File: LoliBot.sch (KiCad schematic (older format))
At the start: 41 parts, among them J1 LOLINBATT, J10 LEFT-MOTOR, J11 REFLECT_, J12 MECH, J13 MECH, J14 MECH, J15 MECH, J16 MECH, J17 MECH, J18 MECH, J19 MECH, J2 APA106, J20 CONN_01X08, J21 CONN_01X06, J3 SERVO1, J4 RIGHT, J5 LEFT, J6 MPU-9250, J7 APA106, J8 APA106, J9 RIGHT-MOTOR, SW1 SPST, U1 LOLIN32-LITE, U2 RT9276, U3 L9110, U4 L9110

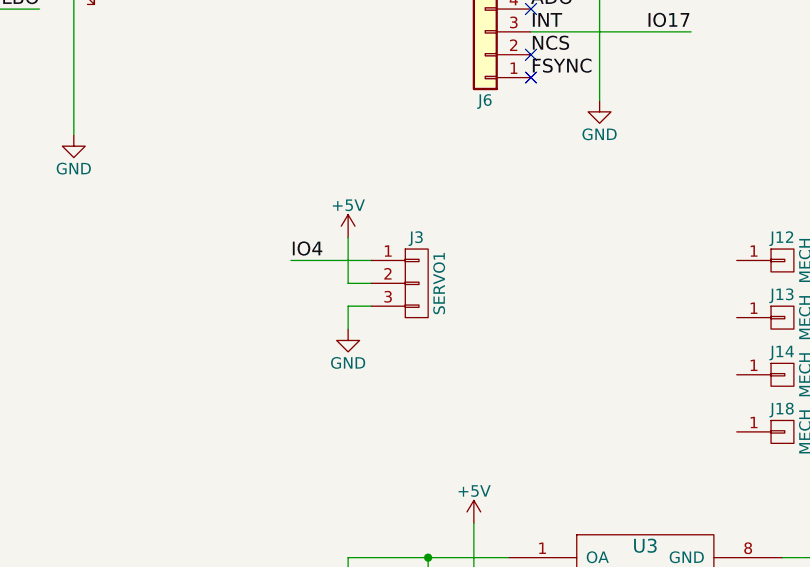
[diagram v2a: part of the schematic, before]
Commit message: Moved Servo position
to remove interference with expansion ports.
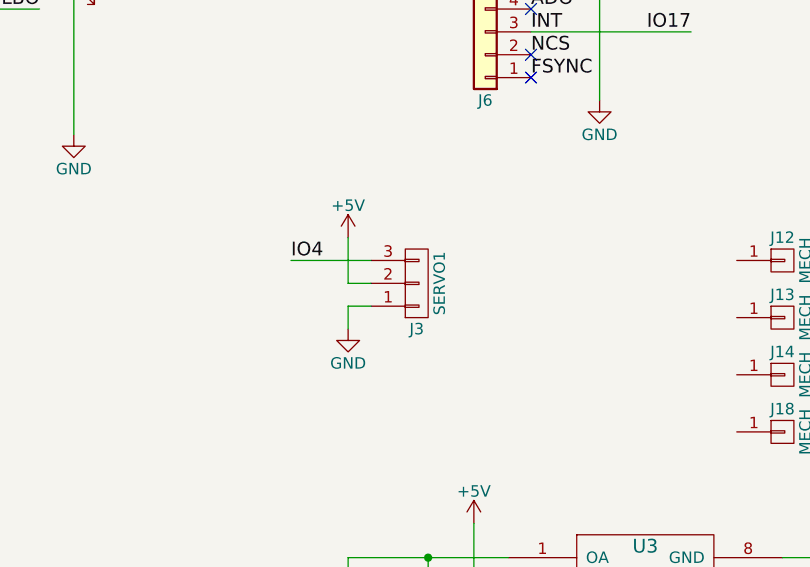
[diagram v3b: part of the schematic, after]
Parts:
- J3: footprint Pin_Headers:Pin_Header_Straight_1x03_Pitch2.54mm -> Pin_Headers:Pin_Header_Angled_1x03_Pitch2.54mm
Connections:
- net GND: now also J3.1 (P1); no longer J3.3 (P3)
- net IO4: now also J3.3 (P3); no longer J3.1 (P1)
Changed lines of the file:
@@
 F 0 "J3" H 8700 3100 50  0000 C CNN
 F 1 "SERVO1" V 8800 2900 50  0000 C CNN
-F 2 "Pin_Headers:Pin_Header_Straight_1x03_Pitch2.54mm" H 8700 2900 50  0001 C CNN
+F 2 "Pin_Headers:Pin_Header_Angled_1x03_Pitch2.54mm" H 8700 2900 50  0001 C CNN
 F 3 "" H 8700 2900 50  0001 C CNN
 	1    8700 2900
-	1    0    0    -1
+	1    0    0    1
 $EndComp
 $Comp

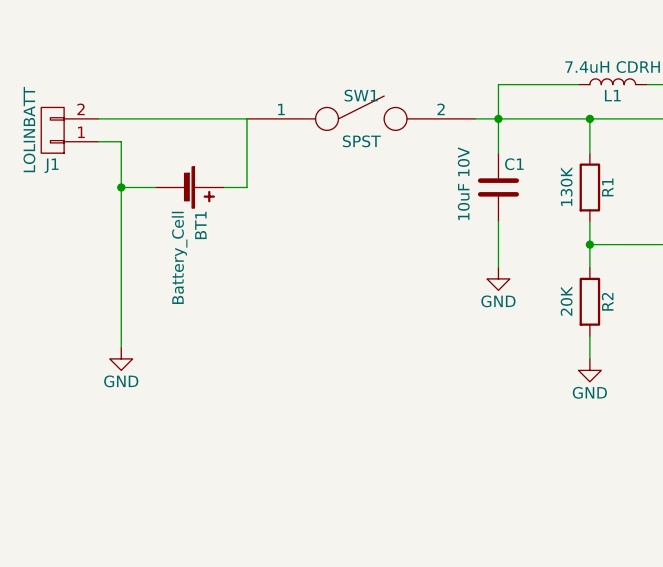
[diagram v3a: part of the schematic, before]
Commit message: battery symbols reversed.
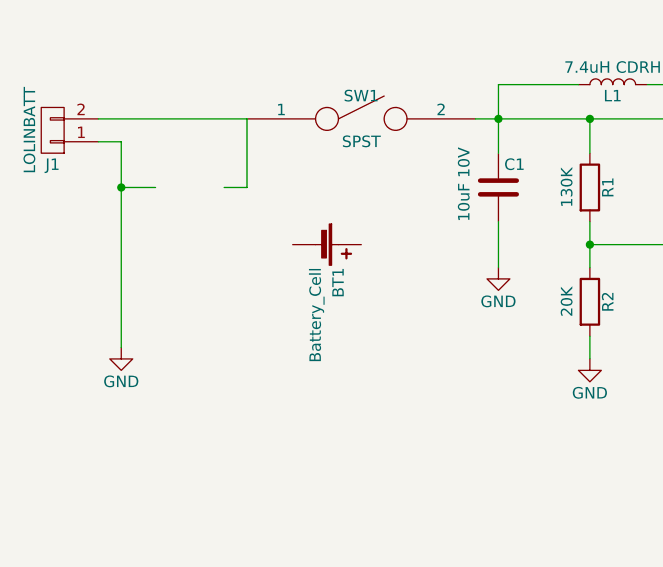
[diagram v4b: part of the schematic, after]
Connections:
- net GND: no longer BT1.2 (-)
- net at J1.2 (P2), SW1.1: no longer BT1.1 (+)
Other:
- moved on the sheet: BT1
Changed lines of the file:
@@
 L Battery_Cell BT1
 U 1 1 59DB5FBF
-P 1500 1450
-F 0 "BT1" H 1600 1550 50  0000 L CNN
-F 1 "Battery_Cell" H 1600 1450 50  0000 L CNN
-F 2 "libs:BH-18650" V 1500 1510 50  0001 C CNN
-F 3 "" V 1500 1510 50  0001 C CNN
-	1    1500 1450
+P 2100 1700
+F 0 "BT1" H 2200 1800 50  0000 L CNN
+F 1 "Battery_Cell" H 2200 1700 50  0000 L CNN
+F 2 "libs:BH-18650" V 2100 1760 50  0001 C CNN
+F 3 "" V 2100 1760 50  0001 C CNN
+	1    2100 1700
 	0    1    1    0
 $EndComp

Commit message: Removed voltage boost.
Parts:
- removed C1: 10uF 10V, Capacitors_SMD:C_1210_HandSoldering, symbol C
- removed C2: 22uF 10V, Capacitors_SMD:C_1210_HandSoldering, symbol C
- removed D1: LOW BATT, LEDs:LED_D3.0mm, symbol LED
- removed L1: 7.4uH CDRH, Choke_SMD:Choke_SMD_7.3x7.3_H3.5, symbol L
- removed R1: 130K, Resistors_SMD:R_0805_HandSoldering, symbol R
- removed R2: 20K, Resistors_SMD:R_0805_HandSoldering, symbol R
- removed R3: 180K 1%, Resistors_SMD:R_0805_HandSoldering, symbol R
- removed R4: 20K 1%, Resistors_SMD:R_0805_HandSoldering, symbol R
- removed R5: 10K, Resistors_SMD:R_0805_HandSoldering, symbol R
- removed R6: 1K, Resistors_SMD:R_0805_HandSoldering, symbol R
- removed U2: RT9276, Housings_DFN_QFN:DFN-10-1EP_3x3mm_Pitch0.5mm, symbol RT9276
- added J22, J23: BRIDGE, Pin_Headers:Pin_Header_Straight_1x02_Pitch2.54mm, symbol CONN_01X02
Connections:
- net GND: now also BT1.2 (-)
- net IO16: now also J3.3 (P3); no longer J11.3 (P3)
- net IO4: now also J11.3 (P3); no longer J3.3 (P3)
- net BATT_V: now reaches J1.2 (P2), SW1.1
- net BATT_V: now also J2.2 (P2), J20.1 (P1), J3.2 (P2), J7.2 (P2), J8.2 (P2), R7.1, J22.1 (P1), J23.1 (P1)
- net at BT1.1 (+): now also SW1.2
- removed net +5V: J2.2 (P2), J20.1 (P1), J3.2 (P2), J7.2 (P2), J8.2 (P2), R7.1, U3.2 (VCC), U3.3 (VCC), U4.2 (VCC), U4.3 (VCC)
- new net: J22.2 (P2), U3.2 (VCC), U3.3 (VCC)
- new net: J23.2 (P2), U4.2 (VCC), U4.3 (VCC)
- no-connect marks 9 -> 16
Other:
- note removed: "Vout = 5.0V\nat 500mA max."
- moved on the sheet: BT1, C4, J5, U4

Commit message: Added Fuse.  Updated pcb
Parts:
- added F1: 1A PTC, Resistors_SMD:R_1210_HandSoldering, symbol Polyfuse
- added J24: FUSE_BRIDGE, libs:bridge, symbol CONN_01X02
- added J25, J26: MECH, Mounting_Holes:MountingHole_3.2mm_M3_Pad, symbol CONN_01X01
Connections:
- net +3V3: no longer J11.1 (P1)
- net IO22: now also J11.1 (P1)
- net at BT1.1 (+): now also F1.2, J24.2 (P2); no longer SW1.2
- new net: F1.1, J24.1 (P1), SW1.2
- no-connect marks 16 -> 18
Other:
- moved on the sheet: J12, J13, J14, J15, J16, J17, J18, J19
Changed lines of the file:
@@
 	1400 1450 1250 1450
 Connection ~ 1250 1450
-Wire Wire Line
-	1700 1450 2850 1450
 $Comp
 L SPST SW1
@@
 	5150 3350 5150 3550
 $Comp
-L GND #PWR012
+L GND #PWR011
 U 1 1 59E30F3C
 P 5150 3550
-F 0 "#PWR012" H 5150 3300 50  0001 C CNN
+F 0 "#PWR011" H 5150 3300 50  0001 C CNN
 F 1 "GND" H 5150 3400 50  0000 C CNN
 F 2 "" H 5150 3550 50  0001 C CNN
@@
 	6100 3350 6100 3550
 $Comp
-L GND #PWR014
+L GND #PWR012
 U 1 1 59F090C3
 P 6100 3550
-F 0 "#PWR014" H 6100 3300 50  0001 C CNN
+F 0 "#PWR012" H 6100 3300 50  0001 C CNN
 F 1 "GND" H 6100 3400 50  0000 C CNN
 F 2 "" H 6100 3550 50  0001 C CNN
@@
 L CONN_01X01 J15
 U 1 1 59F9BFEA
-P 10700 2800
-F 0 "J15" H 10700 2900 50  0000 C CNN
-F 1 "MECH" V 10800 2800 50  0000 C CNN
-F 2 "Mounting_Holes:MountingHole_3.2mm_M3_Pad" H 10700 2800 50  0001 C CNN
-F 3 "" H 10700 2800 50  0001 C CNN
-	1    10700 2800
+P 10700 2900
+F 0 "J15" H 10700 3000 50  0000 C CNN
+F 1 "MECH" V 10800 2900 50  0000 C CNN
+F 2 "Mounting_Holes:MountingHole_3.2mm_M3_Pad" H 10700 2900 50  0001 C CNN
+F 3 "" H 10700 2900 50  0001 C CNN
+	1    10700 2900
 	1    0    0    -1
 $EndComp
@@
 L CONN_01X01 J16
 U 1 1 59F9C210
-P 10700 3050
-F 0 "J16" H 10700 3150 50  0000 C CNN
-F 1 "MECH" V 10800 3050 50  0000 C CNN
-F 2 "Mounting_Holes:MountingHole_3.2mm_M3_Pad" H 10700 3050 50  0001 C CNN
-F 3 "" H 10700 3050 50  0001 C CNN
-	1    10700 3050
+P 10700 3150
+F 0 "J16" H 10700 3250 50  0000 C CNN
+F 1 "MECH" V 10800 3150 50  0000 C CNN
+F 2 "Mounting_Holes:MountingHole_3.2mm_M3_Pad" H 10700 3150 50  0001 C CNN
+F 3 "" H 10700 3150 50  0001 C CNN
+	1    10700 3150
 	1    0    0    -1
 $EndComp
@@
 L CONN_01X01 J12
 U 1 1 59F9C63A
-P 10300 2800
-F 0 "J12" H 10300 2900 50  0000 C CNN
-F 1 "MECH" V 10400 2800 50  0000 C CNN
-F 2 "Mounting_Holes:MountingHole_3.2mm_M3_Pad" H 10300 2800 50  0001 C CNN
-F 3 "" H 10300 2800 50  0001 C CNN
-	1    10300 2800
+P 10300 2900
+F 0 "J12" H 10300 3000 50  0000 C CNN
+F 1 "MECH" V 10400 2900 50  0000 C CNN
+F 2 "Mounting_Holes:MountingHole_3.2mm_M3_Pad" H 10300 2900 50  0001 C CNN
+F 3 "" H 10300 2900 50  0001 C CNN
+	1    10300 2900
 	1    0    0    -1
 $EndComp
@@
 L CONN_01X01 J13
 U 1 1 59F9C640
-P 10300 3050
-F 0 "J13" H 10300 3150 50  0000 C CNN
-F 1 "MECH" V 10400 3050 50  0000 C CNN
-F 2 "Mounting_Holes:MountingHole_3.2mm_M3_Pad" H 10300 3050 50  0001 C CNN
-F 3 "" H 10300 3050 50  0001 C CNN
-	1    10300 3050
+P 10300 3150
+F 0 "J13" H 10300 3250 50  0000 C CNN
+F 1 "MECH" V 10400 3150 50  0000 C CNN
+F 2 "Mounting_Holes:MountingHole_3.2mm_M3_Pad" H 10300 3150 50  0001 C CNN
+F 3 "" H 10300 3150 50  0001 C CNN
+	1    10300 3150
 	1    0    0    -1
 $EndComp
@@
 L CONN_01X01 J17
 U 1 1 59F9C6E4
-P 10700 3300
-F 0 "J17" H 10700 3400 50  0000 C CNN
-F 1 "MECH" V 10800 3300 50  0000 C CNN
-F 2 "Mounting_Holes:MountingHole_3.2mm_M3_Pad" H 10700 3300 50  0001 C CNN
-F 3 "" H 10700 3300 50  0001 C CNN
-	1    10700 3300
+P 10700 3400
+F 0 "J17" H 10700 3500 50  0000 C CNN
+F 1 "MECH" V 10800 3400 50  0000 C CNN
+F 2 "Mounting_Holes:MountingHole_3.2mm_M3_Pad" H 10700 3400 50  0001 C CNN
+F 3 "" H 10700 3400 50  0001 C CNN
+	1    10700 3400
 	1    0    0    -1
 $EndComp
@@
 L CONN_01X01 J14
 U 1 1 59F9C6EA
-P 10300 3300
-F 0 "J14" H 10300 3400 50  0000 C CNN
-F 1 "MECH" V 10400 3300 50  0000 C CNN
-F 2 "Mounting_Holes:MountingHole_3.2mm_M3_Pad" H 10300 3300 50  0001 C CNN
-F 3 "" H 10300 3300 50  0001 C CNN
-	1    10300 3300
+P 10300 3400
+F 0 "J14" H 10300 3500 50  0000 C CNN
+F 1 "MECH" V 10400 3400 50  0000 C CNN
+F 2 "Mounting_Holes:MountingHole_3.2mm_M3_Pad" H 10300 3400 50  0001 C CNN
+F 3 "" H 10300 3400 50  0001 C CNN
+	1    10300 3400
 	1    0    0    -1
 $EndComp
@@
 $EndComp
 $Comp
-L +3.3V #PWR015
-U 1 1 59F9D53B
-P 7150 5450
-F 0 "#PWR015" H 7150 5300 50  0001 C CNN
-F 1 "+3.3V" H 7150 5590 50  0000 C CNN
-F 2 "" H 7150 5450 50  0001 C CNN
-F 3 "" H 7150 5450 50  0001 C CNN
-	1    7150 5450
-	1    0    0    -1
-$EndComp
-$Comp
-L GND #PWR016
+L GND #PWR013
 U 1 1 59F9DB04
 P 7200 5850
-F 0 "#PWR016" H 7200 5600 50  0001 C CNN
+F 0 "#PWR013" H 7200 5600 50  0001 C CNN
 F 1 "GND" H 7200 5700 50  0000 C CNN
 F 2 "" H 7200 5850 50  0001 C CNN
@@
 $EndComp
 Wire Wire Line
-	7100 5500 7150 5500
-Wire Wire Line
-	7150 5500 7150 5450
-Wire Wire Line
 	7100 5600 7200 5600
 Wire Wire Line
@@
 L CONN_01X01 J19
 U 1 1 59F9F795
-P 10700 3550
-F 0 "J19" H 10700 3650 50  0000 C CNN
-F 1 "MECH" V 10800 3550 50  0000 C CNN
-F 2 "Mounting_Holes:MountingHole_3.2mm_M3_Pad" H 10700 3550 50  0001 C CNN
-F 3 "" H 10700 3550 50  0001 C CNN
-	1    10700 3550
+P 10700 3650
+F 0 "J19" H 10700 3750 50  0000 C CNN
+F 1 "MECH" V 10800 3650 50  0000 C CNN
+F 2 "Mounting_Holes:MountingHole_3.2mm_M3_Pad" H 10700 3650 50  0001 C CNN
+F 3 "" H 10700 3650 50  0001 C CNN
+	1    10700 3650
 	1    0    0    -1
 $EndComp
@@
 L CONN_01X01 J18
 U 1 1 59F9F79B
-P 10300 3550
-F 0 "J18" H 10300 3650 50  0000 C CNN
-F 1 "MECH" V 10400 3550 50  0000 C CNN
-F 2 "Mounting_Holes:MountingHole_3.2mm_M3_Pad" H 10300 3550 50  0001 C CNN
-F 3 "" H 10300 3550 50  0001 C CNN
-	1    10300 3550
+P 10300 3650
+F 0 "J18" H 10300 3750 50  0000 C CNN
+F 1 "MECH" V 10400 3650 50  0000 C CNN
+F 2 "Mounting_Holes:MountingHole_3.2mm_M3_Pad" H 10300 3650 50  0001 C CNN
+F 3 "" H 10300 3650 50  0001 C CNN
+	1    10300 3650
 	1    0    0    -1
 $EndComp
@@
 $EndComp
 $Comp
-L +3.3V #PWR017
+L +3.3V #PWR014
 U 1 1 5A117D1F
 P 5200 5850
-F 0 "#PWR017" H 5200 5700 50  0001 C CNN
+F 0 "#PWR014" H 5200 5700 50  0001 C CNN
 F 1 "+3.3V" H 5200 5990 50  0000 C CNN
 F 2 "" H 5200 5850 50  0001 C CNN
@@
 IO33
 $Comp
-L GND #PWR018
+L GND #PWR015
 U 1 1 5A1181BF
 P 5200 5100
-F 0 "#PWR018" H 5200 4850 50  0001 C CNN
+F 0 "#PWR015" H 5200 4850 50  0001 C CNN
 F 1 "GND" H 5200 4950 50  0000 C CNN
 F 2 "" H 5200 5100 50  0001 C CNN
@@
 Wire Wire Line
 	5100 6450 5350 6450
-NoConn ~ 10500 2800
-NoConn ~ 10500 3050
-NoConn ~ 10500 3300
-NoConn ~ 10500 3550
-NoConn ~ 10100 3550
-NoConn ~ 10100 3300
-NoConn ~ 10100 3050
-NoConn ~ 10100 2800
+NoConn ~ 10500 2900
+NoConn ~ 10500 3150
+NoConn ~ 10500 3400
+NoConn ~ 10500 3650
+NoConn ~ 10100 3650
+NoConn ~ 10100 3400
+NoConn ~ 10100 3150
+NoConn ~ 10100 2900
 $Comp
 L CONN_01X02 J22
@@
 Connection ~ 4200 3450
 Connection ~ 5050 3450
+$Comp
+L CONN_01X01 J26
+U 1 1 5A23FA6B
+P 10700 2650
+F 0 "J26" H 10700 2750 50  0000 C CNN
+F 1 "MECH" V 10800 2650 50  0000 C CNN
+F 2 "Mounting_Holes:MountingHole_3.2mm_M3_Pad" H 10700 2650 50  0001 C CNN
+F 3 "" H 10700 2650 50  0001 C CNN
+	1    10700 2650
+	1    0    0    -1
+$EndComp
+$Comp
+L CONN_01X01 J25
+U 1 1 5A23FA71
+P 10300 2650
+F 0 "J25" H 10300 2750 50  0000 C CNN
+F 1 "MECH" V 10400 2650 50  0000 C CNN
+F 2 "Mounting_Holes:MountingHole_3.2mm_M3_Pad" H 10300 2650 50  0001 C CNN
+F 3 "" H 10300 2650 50  0001 C CNN
+	1    10300 2650
+	1    0    0    -1
+$EndComp
+NoConn ~ 10500 2650
+NoConn ~ 10100 2650
+Wire Wire Line
+	7100 5500 7450 5500
+$Comp
+L Polyfuse F1
+U 1 1 5A2933C9
+P 2050 1450
+F 0 "F1" V 1950 1450 50  0000 C CNN
+F 1 "1A PTC" V 2150 1450 50  0000 C CNN
+F 2 "Resistors_SMD:R_1210_HandSoldering" H 2100 1250 50  0001 L CNN
+F 3 "" H 2050 1450 50  0001 C CNN
+	1    2050 1450
+	0    1    1    0
+$EndComp
+Wire Wire Line
+	2850 1450 2200 1450
+Wire Wire Line
+	1900 1450 1700 1450
+$Comp
+L CONN_01X02 J24
+U 1 1 5A29363E
+P 2050 1950
+F 0 "J24" H 2050 2100 50  0000 C CNN
+F 1 "FUSE_BRIDGE" V 2150 1950 50  0000 C CNN
+F 2 "libs:bridge" H 2050 1950 50  0001 C CNN
+F 3 "" H 2050 1950 50  0001 C CNN
+	1    2050 1950
+	0    1    1    0
+$EndComp
+Wire Wire Line
+	1800 1450 1800 1700
+Wire Wire Line
+	1800 1700 2000 1700
+Wire Wire Line
+	2000 1700 2000 1750
+Connection ~ 1800 1450
+Wire Wire Line
+	2300 1450 2300 1700
+Wire Wire Line
+	2300 1700 2100 1700
+Wire Wire Line
+	2100 1700 2100 1750
+Connection ~ 2300 1450
+Text Label 7450 5500 2    60   ~ 0
+IO22
 $EndSCHEMATC

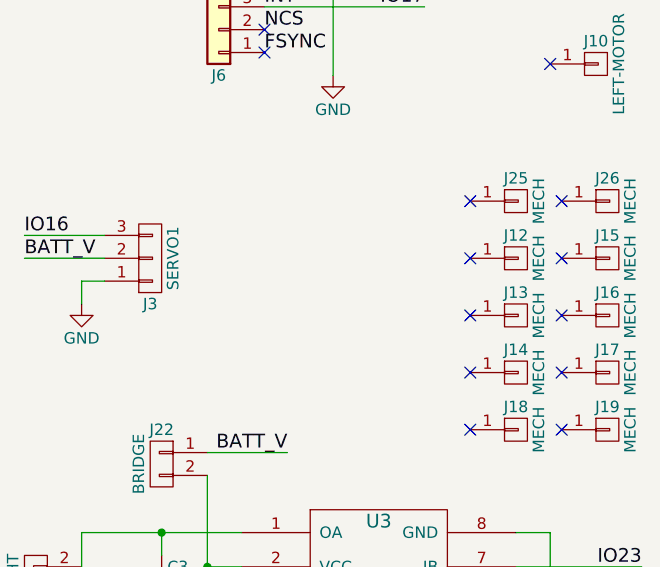
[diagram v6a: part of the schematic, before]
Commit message: Added Through holes for cable ties
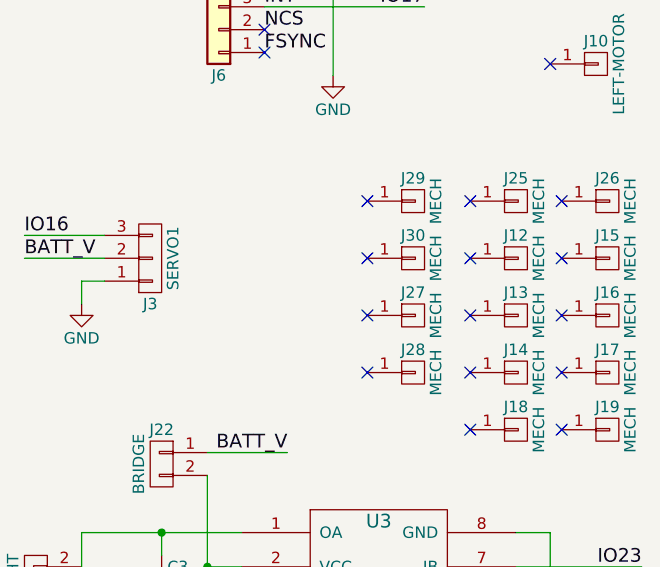
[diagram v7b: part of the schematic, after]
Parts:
- added J27, J28, J29, J30: MECH, Mounting_Holes:MountingHole_3.2mm_M3_Pad, symbol CONN_01X01
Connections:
- no-connect marks 18 -> 22
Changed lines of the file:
@@
 $EndComp
 $Comp
-L GND #PWR01
+L GND #PWR1
 U 1 1 59DB6136
 P 1250 2150
-F 0 "#PWR01" H 1250 1900 50  0001 C CNN
+F 0 "#PWR1" H 1250 1900 50  0001 C CNN
 F 1 "GND" H 1250 2000 50  0000 C CNN
 F 2 "" H 1250 2150 50  0001 C CNN
@@
 $EndComp
 $Comp
-L GND #PWR02
+L GND #PWR9
 U 1 1 59DB834E
 P 7200 1800
-F 0 "#PWR02" H 7200 1550 50  0001 C CNN
+F 0 "#PWR9" H 7200 1550 50  0001 C CNN
 F 1 "GND" H 7200 1650 50  0000 C CNN
 F 2 "" H 7200 1800 50  0001 C CNN
@@
 $EndComp
 $Comp
-L GND #PWR03
+L GND #PWR4
 U 1 1 59DBA675
 P 4300 3550
-F 0 "#PWR03" H 4300 3300 50  0001 C CNN
+F 0 "#PWR4" H 4300 3300 50  0001 C CNN
 F 1 "GND" H 4300 3400 50  0000 C CNN
 F 2 "" H 4300 3550 50  0001 C CNN
@@
 $EndComp
 $Comp
-L GND #PWR04
+L GND #PWR14
 U 1 1 59DBB61B
 P 10450 4750
-F 0 "#PWR04" H 10450 4500 50  0001 C CNN
+F 0 "#PWR14" H 10450 4500 50  0001 C CNN
 F 1 "GND" H 10450 4600 50  0000 C CNN
 F 2 "" H 10450 4750 50  0001 C CNN
@@
 $EndComp
 $Comp
-L GND #PWR05
+L GND #PWR15
 U 1 1 59DBCDC3
 P 10500 6200
-F 0 "#PWR05" H 10500 5950 50  0001 C CNN
+F 0 "#PWR15" H 10500 5950 50  0001 C CNN
 F 1 "GND" H 10500 6050 50  0000 C CNN
 F 2 "" H 10500 6200 50  0001 C CNN
@@
 $EndComp
 $Comp
-L GND #PWR06
+L GND #PWR11
 U 1 1 59DBDB38
 P 8400 3100
-F 0 "#PWR06" H 8400 2850 50  0001 C CNN
+F 0 "#PWR11" H 8400 2850 50  0001 C CNN
 F 1 "GND" H 8400 2950 50  0000 C CNN
 F 2 "" H 8400 3100 50  0001 C CNN
@@
 IO13
 $Comp
-L +3.3V #PWR07
+L +3.3V #PWR3
 U 1 1 59DC0699
 P 3300 4450
-F 0 "#PWR07" H 3300 4300 50  0001 C CNN
+F 0 "#PWR3" H 3300 4300 50  0001 C CNN
 F 1 "+3.3V" H 3300 4590 50  0000 C CNN
 F 2 "" H 3300 4450 50  0001 C CNN
@@
 $EndComp
 $Comp
-L GND #PWR08
+L GND #PWR2
 U 1 1 59DC0B2B
 P 1300 6000
-F 0 "#PWR08" H 1300 5750 50  0001 C CNN
+F 0 "#PWR2" H 1300 5750 50  0001 C CNN
 F 1 "GND" H 1300 5850 50  0000 C CNN
 F 2 "" H 1300 6000 50  0001 C CNN
@@
 FSYNC
 $Comp
-L +3.3V #PWR09
+L +3.3V #PWR12
 U 1 1 59E28F97
 P 9500 800
-F 0 "#PWR09" H 9500 650 50  0001 C CNN
+F 0 "#PWR12" H 9500 650 50  0001 C CNN
 F 1 "+3.3V" H 9500 940 50  0000 C CNN
 F 2 "" H 9500 800 50  0001 C CNN
@@
 	9500 1100 9500 800
 $Comp
-L GND #PWR010
+L GND #PWR13
 U 1 1 59E29073
 P 9500 2100
-F 0 "#PWR010" H 9500 1850 50  0001 C CNN
+F 0 "#PWR13" H 9500 1850 50  0001 C CNN
 F 1 "GND" H 9500 1950 50  0000 C CNN
 F 2 "" H 9500 2100 50  0001 C CNN
@@
 	5150 3350 5150 3550
 $Comp
-L GND #PWR011
+L GND #PWR5
 U 1 1 59E30F3C
 P 5150 3550
-F 0 "#PWR011" H 5150 3300 50  0001 C CNN
+F 0 "#PWR5" H 5150 3300 50  0001 C CNN
 F 1 "GND" H 5150 3400 50  0000 C CNN
 F 2 "" H 5150 3550 50  0001 C CNN
@@
 	6100 3350 6100 3550
 $Comp
-L GND #PWR012
+L GND #PWR8
 U 1 1 59F090C3
 P 6100 3550
-F 0 "#PWR012" H 6100 3300 50  0001 C CNN
+F 0 "#PWR8" H 6100 3300 50  0001 C CNN
 F 1 "GND" H 6100 3400 50  0000 C CNN
 F 2 "" H 6100 3550 50  0001 C CNN
@@
 $EndComp
 $Comp
-L GND #PWR013
+L GND #PWR10
 U 1 1 59F9DB04
 P 7200 5850
-F 0 "#PWR013" H 7200 5600 50  0001 C CNN
+F 0 "#PWR10" H 7200 5600 50  0001 C CNN
 F 1 "GND" H 7200 5700 50  0000 C CNN
 F 2 "" H 7200 5850 50  0001 C CNN
@@
 $EndComp
 $Comp
-L +3.3V #PWR014
+L +3.3V #PWR7
 U 1 1 5A117D1F
 P 5200 5850
-F 0 "#PWR014" H 5200 5700 50  0001 C CNN
+F 0 "#PWR7" H 5200 5700 50  0001 C CNN
 F 1 "+3.3V" H 5200 5990 50  0000 C CNN
 F 2 "" H 5200 5850 50  0001 C CNN
@@
 IO33
 $Comp
-L GND #PWR015
+L GND #PWR6
 U 1 1 5A1181BF
 P 5200 5100
-F 0 "#PWR015" H 5200 4850 50  0001 C CNN
+F 0 "#PWR6" H 5200 4850 50  0001 C CNN
 F 1 "GND" H 5200 4950 50  0000 C CNN
 F 2 "" H 5200 5100 50  0001 C CNN
@@
 Text Label 7450 5500 2    60   ~ 0
 IO22
+$Comp
+L CONN_01X01 J27
+U 1 1 5A295800
+P 9850 3150
+F 0 "J27" H 9850 3250 50  0000 C CNN
+F 1 "MECH" V 9950 3150 50  0000 C CNN
+F 2 "Mounting_Holes:MountingHole_3.2mm_M3_Pad" H 9850 3150 50  0001 C CNN
+F 3 "" H 9850 3150 50  0001 C CNN
+	1    9850 3150
+	1    0    0    -1
+$EndComp
+$Comp
+L CONN_01X01 J28
+U 1 1 5A29588D
+P 9850 3400
+F 0 "J28" H 9850 3500 50  0000 C CNN
+F 1 "MECH" V 9950 3400 50  0000 C CNN
+F 2 "Mounting_Holes:MountingHole_3.2mm_M3_Pad" H 9850 3400 50  0001 C CNN
+F 3 "" H 9850 3400 50  0001 C CNN
+	1    9850 3400
+	1    0    0    -1
+$EndComp
+NoConn ~ 9650 3150
+NoConn ~ 9650 3400
+$Comp
+L CONN_01X01 J29
+U 1 1 5A295C52
+P 9850 2650
+F 0 "J29" H 9850 2750 50  0000 C CNN
+F 1 "MECH" V 9950 2650 50  0000 C CNN
+F 2 "Mounting_Holes:MountingHole_3.2mm_M3_Pad" H 9850 2650 50  0001 C CNN
+F 3 "" H 9850 2650 50  0001 C CNN
+	1    9850 2650
+	1    0    0    -1
+$EndComp
+$Comp
+L CONN_01X01 J30
+U 1 1 5A295C58
+P 9850 2900
+F 0 "J30" H 9850 3000 50  0000 C CNN
+F 1 "MECH" V 9950 2900 50  0000 C CNN
+F 2 "Mounting_Holes:MountingHole_3.2mm_M3_Pad" H 9850 2900 50  0001 C CNN
+F 3 "" H 9850 2900 50  0001 C CNN
+	1    9850 2900
+	1    0    0    -1
+$EndComp
+NoConn ~ 9650 2650
+NoConn ~ 9650 2900
 $EndSCHEMATC
